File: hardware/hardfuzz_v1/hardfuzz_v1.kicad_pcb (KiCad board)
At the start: 2 copper layers, 174 x 80.3 mm, 68 parts, among them J1 USB-C, J2 Qwiic, J3 BUS, J4 SPI/UART, J5 CAN, SW1 PROG, U1 XC7A35T-CSG324, U10 TXS0108EPW, U2 FT2232HQ, U3 MX25L3233F, U6 TLV62566, U7 TLV62566, U8 AP2112K-1.8, U9 SN65HVD230, Y1 12MHz, Y2 12MHz

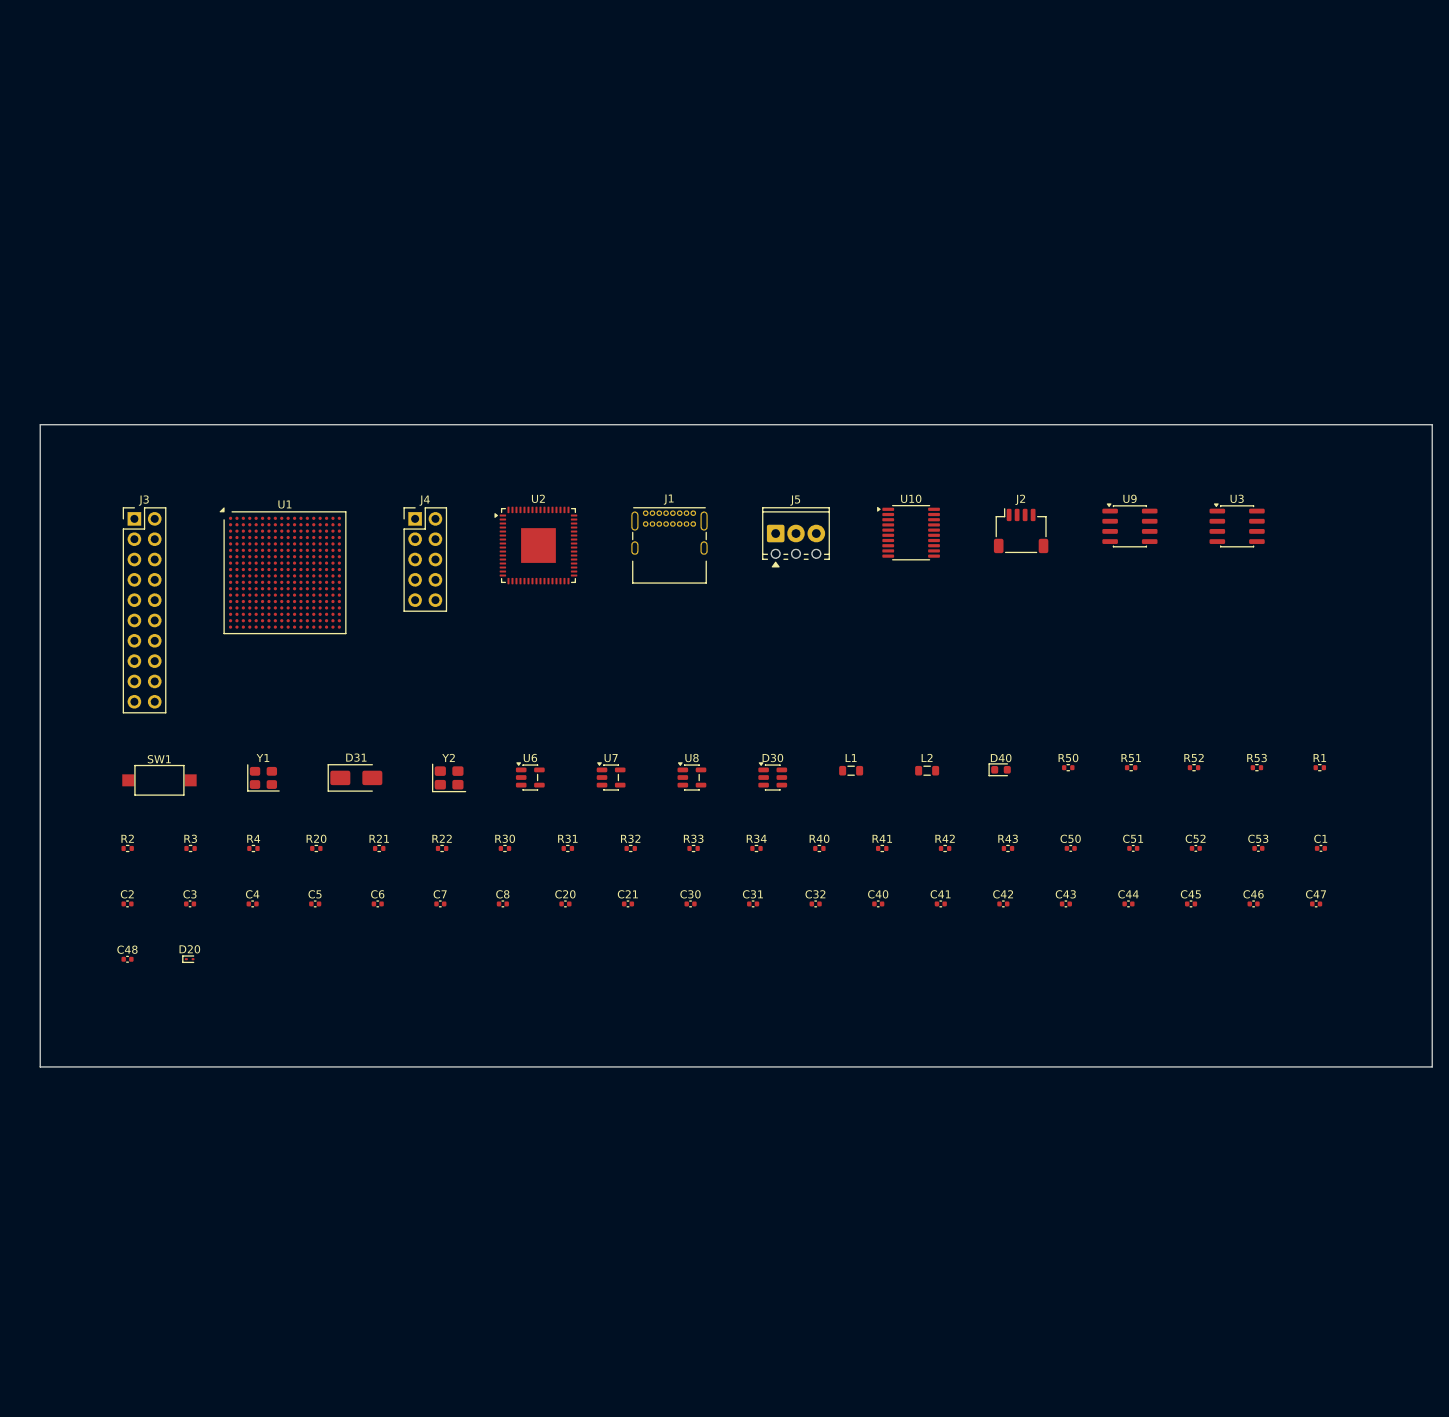
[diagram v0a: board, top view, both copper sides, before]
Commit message: v2: standalone/BLE architecture doc + ESP32 controller added to the board
docs/HardFuzz_v2_Standalone.md: computer-free architecture — an on-board ESP32-S3
runs the header-only C++ campaign engine (ports nearly as-is), arms the FPGA over
UART, drives the DUT, and streams results to a phone app over BLE. Includes the GATT
service definition and the host-engine -> ESP32 mapping.

Design: gen/esp32_sheet.py adds the ESP32-S3-WROOM-1 (power, EN/IO0 boot circuits,
UART to FPGA via the freed FT2232 ch-B control nets, UART to a DUT header, USB-C for
programming, BLE LED). Regenerated schematic (7 sheets, 83 parts) + PCB (loads,
ESP32 placed). FT2232 keeps JTAG; ESP32 owns the runtime control path.

Co-Authored-By: Claude Opus 4.8 <noreply@anthropic.com>
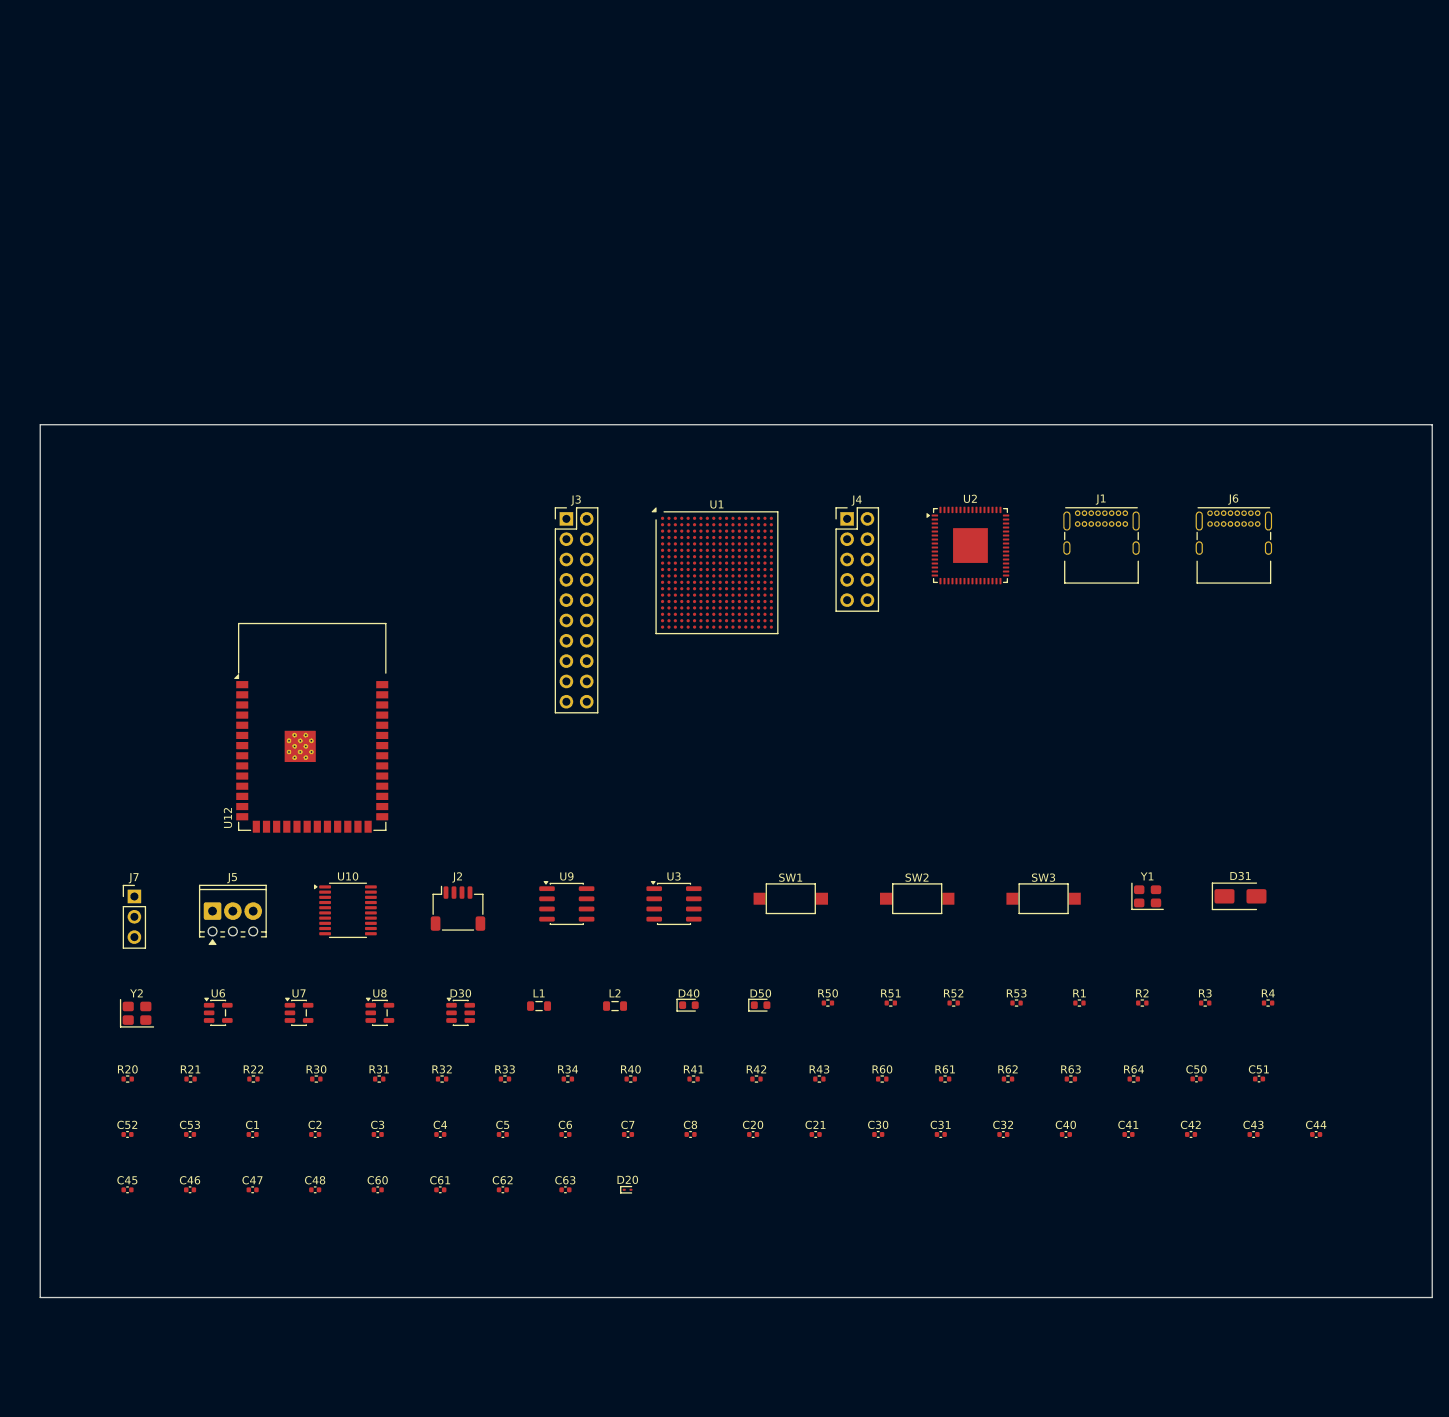
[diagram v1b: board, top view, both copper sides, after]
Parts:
- added C60: 10uF, Capacitor_SMD:C_0402_1005Metric, F.Cu at (45.2, 98.6)
- added C61: 100nF, Capacitor_SMD:C_0402_1005Metric, F.Cu at (53.0, 98.6)
- added C62: 1uF, Capacitor_SMD:C_0402_1005Metric, F.Cu at (60.8, 98.6)
- added C63: 10uF, Capacitor_SMD:C_0402_1005Metric, F.Cu at (68.7, 98.6)
- added D50: BLE, LED_SMD:LED_0603_1608Metric, F.Cu at (93.0, 75.6)
- added J6: USB-C, Connector_USB:USB_C_Receptacle_GCT_USB4085, F.Cu at (149.2, 14.1)
- added J7: DUT, Connector_PinHeader_2.54mm:PinHeader_1x03_P2.54mm_Vertical, F.Cu at (14.8, 62.0)
- added R60: 10k, Resistor_SMD:R_0402_1005Metric, F.Cu at (108.2, 84.8)
- added R61: 10k, Resistor_SMD:R_0402_1005Metric, F.Cu at (116.1, 84.8)
- added R62: 330, Resistor_SMD:R_0402_1005Metric, F.Cu at (124.0, 84.8)
- added R63: 5.1k, Resistor_SMD:R_0402_1005Metric, F.Cu at (131.8, 84.8)
- added R64: 5.1k, Resistor_SMD:R_0402_1005Metric, F.Cu at (139.7, 84.8)
- added SW2: RST, Button_Switch_SMD:SW_SPST_CK_RS282G05A3, F.Cu at (112.6, 62.2)
- added SW3: BOOT, Button_Switch_SMD:SW_SPST_CK_RS282G05A3, F.Cu at (128.4, 62.2)
- added U12: ESP32-S3-WROOM-1, RF_Module:ESP32-S3-WROOM-1, F.Cu at (37.0, 40.8)
- moved C53 138.2 mm to (21.7, 91.7)
- moved C1 138.2 mm to (29.6, 91.7)
- moved C52 138.2 mm to (13.9, 91.7)
- moved C45 137.7 mm to (13.9, 98.6)
- moved C46 137.7 mm to (21.7, 98.6)
- moved C47 137.7 mm to (29.6, 98.6)
- moved R3 128.3 mm to (148.6, 75.3)
- moved R2 128.3 mm to (140.8, 75.3)
- moved R4 128.3 mm to (156.5, 75.3)
- moved D31 111.5 mm to (153.0, 62.0)
- moved Y1 111.5 mm to (141.4, 62.0)
- moved J5 84.8 mm to (24.5, 63.8)
- moved U10 84.8 mm to (41.5, 63.7)
- moved U3 84.8 mm to (82.2, 62.9)
- moved U9 84.8 mm to (68.8, 62.9)
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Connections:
- U2 pad 38: HOST_TXD -> unconnected-(U2-BDBUS0-Pad38)
- U2 pad 39: HOST_RXD -> unconnected-(U2-BDBUS1-Pad39)
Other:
- board size 174 x 80.3 mm -> 174 x 109.1 mm

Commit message: hardware(pcb): steps 1-4 via pcbnew API — 4-layer, grouped placement, outline, planes
gen/pcb_layout.py drives KiCad's pcbnew API (valid by construction) to do the PCB
bring-up prep: 4-layer stackup, placement grouped by subsystem (from netlist
sheetpaths, decoupling caps clustered with their ICs), board outline sized to fit,
and GND(In1)/+3V3(In2) planes. Runs in two processes (LoadBoard works once per
process; zone-ops after SetCopperLayerCount segfault in-session) and needs a wxApp
for headless zone ops. Board is now 174x173mm, 4 layers, 2 planes.

Left for the GUI: press B to pour zones, add 4 mounting holes, net-class/rule setup,
and routing (step 5).

Co-Authored-By: Claude Opus 4.8 <noreply@anthropic.com>
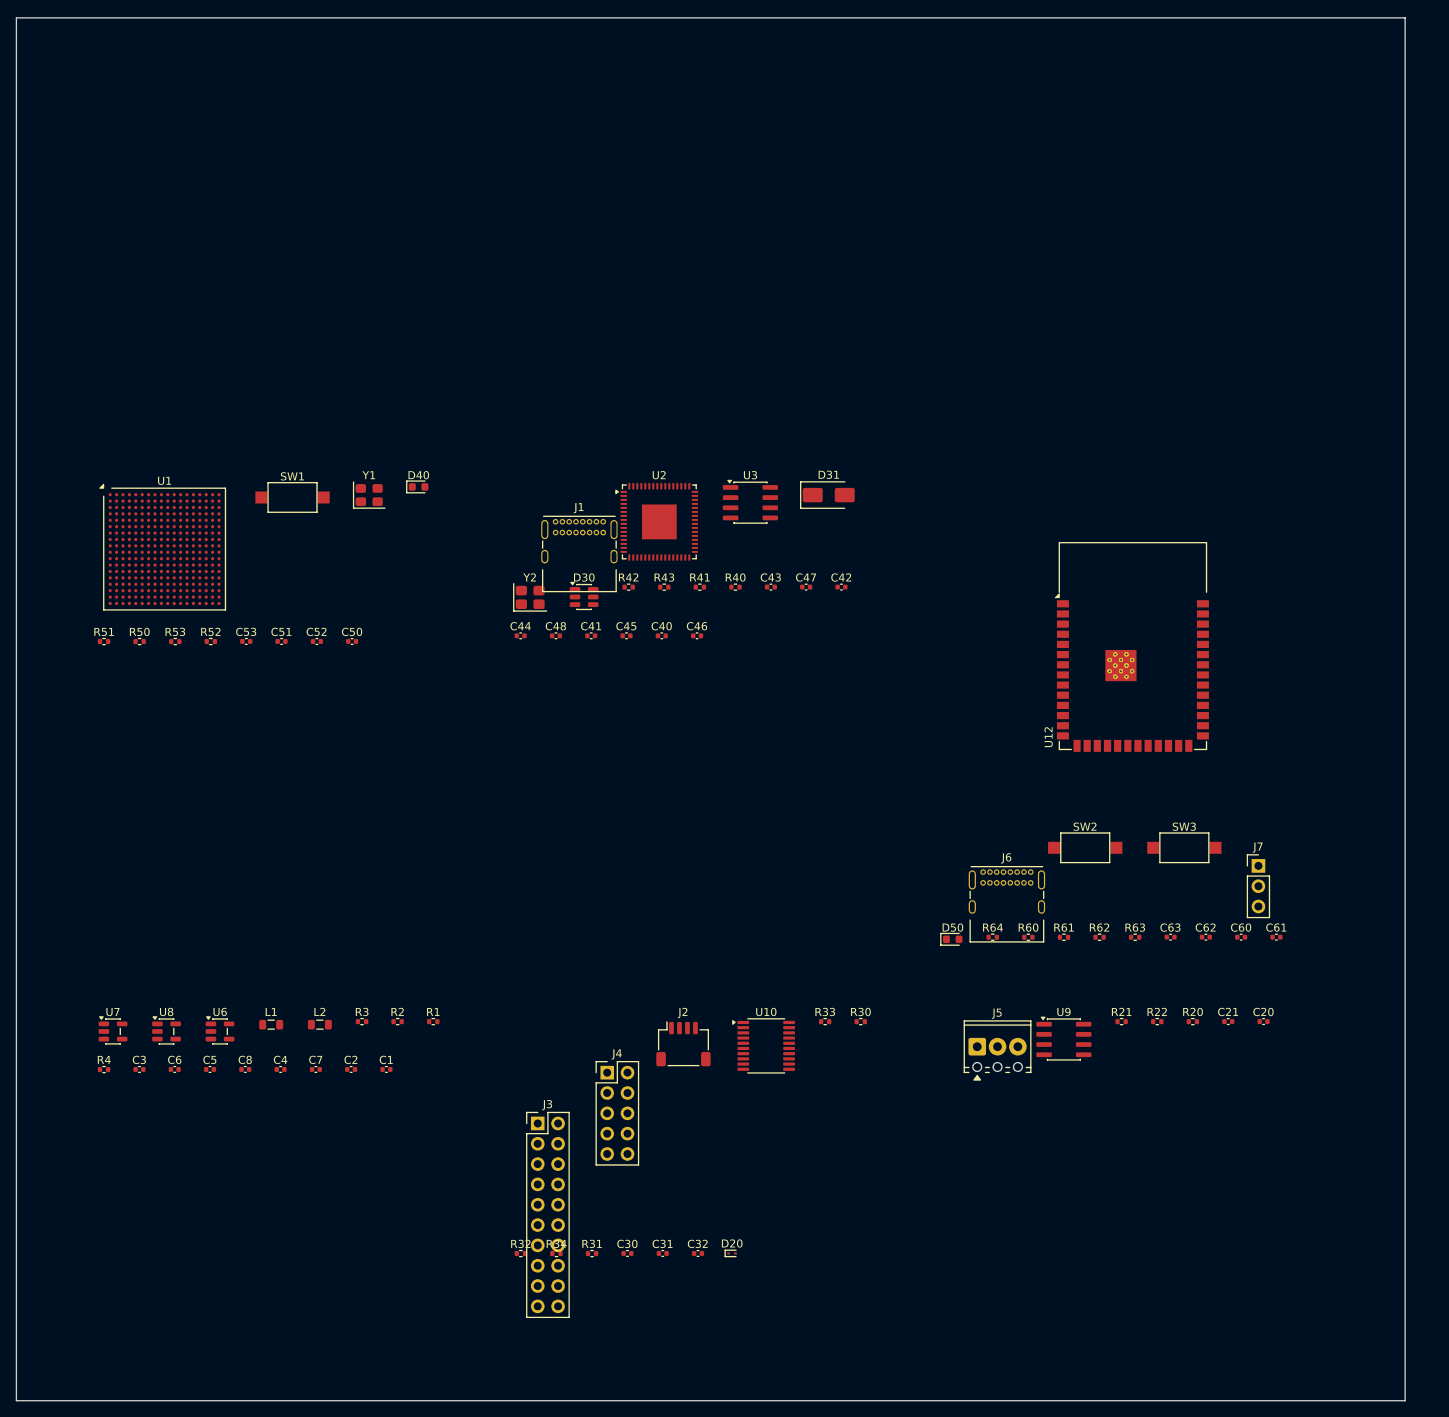
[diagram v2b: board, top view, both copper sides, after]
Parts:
- moved R4 145.7 mm to (11.0, 83.6)
- moved J7 140.6 mm to (155.3, 58.1)
- moved C51 133.9 mm to (33.2, 30.1)
- moved R20 133.3 mm to (147.1, 77.6)
- moved C50 118.9 mm to (42.0, 30.1)
- moved C44 117.4 mm to (63.1, 29.4)
- moved R21 116.6 mm to (138.2, 77.6)
- moved R53 114.5 mm to (19.9, 30.1)
- moved R22 113.2 mm to (142.6, 77.6)
- moved C60 112.5 mm to (153.1, 67.1)
- moved Y1 109.5 mm to (44.1, 11.8)
- moved C61 109.2 mm to (157.5, 67.1)
- moved R51 108.2 mm to (11.0, 30.1)
- moved R3 105.4 mm to (43.2, 77.6)
- moved R52 103.3 mm to (24.3, 30.1)
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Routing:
- added copper zone on In2.Cu, net +3V3
- added copper zone on In1.Cu, net GND
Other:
- board size 174 x 109.1 mm -> 173.6 x 172.9 mm
- copper layers 2 -> 4

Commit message: hardware(pcb): finish steps 1-4 — pour planes, mounting holes, net classes + rules
pcb_layout.py now chains four passes (each its own process): grouped placement +
4-layer + outline, then planes, then pour, then mounting holes. Poured GND/+3V3
planes drop unconnected 363->332. Added the Power net class (+*/GND patterns,
0.4mm tracks / 0.8mm vias) and relaxed rules (0.45/0.25 vias, 0.15 tracks) to the
project file for the BGA fanout. Board is fully bring-up-ready except routing.

Co-Authored-By: Claude Opus 4.8 <noreply@anthropic.com>
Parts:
- added H1: MountingHole_2.2mm_M2, MountingHole_2.2mm_M2, F.Cu at (3.97, -43.9)
- added H2: MountingHole_2.2mm_M2, MountingHole_2.2mm_M2, F.Cu at (169.7, -43.9)
- added H3: MountingHole_2.2mm_M2, MountingHole_2.2mm_M2, F.Cu at (169.7, 121.0)
- added H4: MountingHole_2.2mm_M2, MountingHole_2.2mm_M2, F.Cu at (3.97, 121.0)
